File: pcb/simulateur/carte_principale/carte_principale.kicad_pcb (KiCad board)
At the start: 2 copper layers, 54.5 x 50 mm, 25 parts, among them J1 Arduino_UNO_R3, J2 Conn_01x02, J3 Conn_01x02, P1 TE-FFC-10-0.5, P2 TE-FFC-10-0.5, U1 ESP-WROOM-02, U2 LSM6DS3, U3 BMP280, U5 74AHC1G125, U6 74LS166, U7 LIS2MDL

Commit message: carte principale simulateur en cours
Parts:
- removed C10: 220nF, Capacitor_SMD:C_1206_3216Metric
- removed JP1, JP2, JP3: SJ, Jumper:SolderJumper-2_P1.3mm_Open_RoundedPad1.0x1.5mm
- removed P1, P2: TE-FFC-10-0.5, Insa:FFC-10-0.5
- removed R1, R2: 10K, Resistor_SMD:R_1206_3216Metric
- added C8: 100nF, Capacitor_SMD:C_1206_3216Metric_Pad1.42x1.75mm_HandSolder, F.Cu at (126.0, 92.5)
- added C9: 100nF, Capacitor_SMD:C_1206_3216Metric_Pad1.42x1.75mm_HandSolder, F.Cu at (109.0, 79.5)
- added D1: CSA2D-E3/I, Diode_SMD:D_SMA_Handsoldering, F.Cu at (101.0, 100.0)
- added D2: 3.3V, Diode_SMD:D_SMA_Handsoldering, F.Cu at (129.5, 80.0)
- added F1: Littefuse 72R075U, Capacitor_THT:C_Disc_D7.0mm_W2.5mm_P5.00mm, F.Cu at (98.5, 104.0)
- added R10: 1.5K, Resistor_SMD:R_1206_3216Metric_Pad1.42x1.75mm_HandSolder, F.Cu at (132.0, 90.0)
- added R11: 1.5K, Resistor_SMD:R_1206_3216Metric_Pad1.42x1.75mm_HandSolder, F.Cu at (127.5, 83.5)
- added R12: 100, Resistor_SMD:R_1206_3216Metric_Pad1.42x1.75mm_HandSolder, F.Cu at (104.0, 91.0)
- added R13: 100, Resistor_SMD:R_1206_3216Metric_Pad1.42x1.75mm_HandSolder, F.Cu at (110.0, 92.0)
- added R14: 100, Resistor_SMD:R_1206_3216Metric_Pad1.42x1.75mm_HandSolder, F.Cu at (110.0, 85.5)
- added R15: 100, Resistor_SMD:R_1206_3216Metric_Pad1.42x1.75mm_HandSolder, F.Cu at (109.0, 82.0)
- added R16: 100, Resistor_SMD:R_1206_3216Metric_Pad1.42x1.75mm_HandSolder, F.Cu at (134.5, 94.0)
- added R17: 100, Resistor_SMD:R_1206_3216Metric_Pad1.42x1.75mm_HandSolder, F.Cu at (134.5, 96.5)
- added R18: 100, Resistor_SMD:R_1206_3216Metric_Pad1.42x1.75mm_HandSolder, F.Cu at (116.0, 83.0)
- added R19: 100, Resistor_SMD:R_1206_3216Metric_Pad1.42x1.75mm_HandSolder, F.Cu at (122.0, 81.0)
- added R3: 16K, Resistor_SMD:R_1206_3216Metric_Pad1.42x1.75mm_HandSolder, F.Cu at (128.0, 104.0)
- added R4: 330, Resistor_SMD:R_1206_3216Metric_Pad1.42x1.75mm_HandSolder, F.Cu at (118.5, 99.5)
- added R5: 1K, Resistor_SMD:R_1206_3216Metric_Pad1.42x1.75mm_HandSolder, F.Cu at (132.5, 84.0)
- added R6: 1K, Resistor_SMD:R_1206_3216Metric_Pad1.42x1.75mm_HandSolder, F.Cu at (136.5, 78.0)
- added R7: 100, Resistor_SMD:R_1206_3216Metric_Pad1.42x1.75mm_HandSolder, F.Cu at (133.0, 87.0)
- added R8: 1.5K, Resistor_SMD:R_1206_3216Metric_Pad1.42x1.75mm_HandSolder, F.Cu at (127.5, 89.0)
- added R9: 1.5K, Resistor_SMD:R_1206_3216Metric_Pad1.42x1.75mm_HandSolder, F.Cu at (127.0, 85.5)
- added U4: 74LVC2G17, Package_TO_SOT_SMD:SOT-23-6_Handsoldering, F.Cu at (103.5, 87.0)
- C1: value 100nF -> 10µF; footprint Capacitor_SMD:C_1206_3216Metric -> Capacitor_Tantalum_SMD:CP_EIA-3528-21_Kemet-B_Pad1.50x2.35mm_HandSolder
- C2: value 100nF -> 100µF; footprint Capacitor_SMD:C_1206_3216Metric -> Capacitor_Tantalum_SMD:CP_EIA-3528-21_Kemet-B_Pad1.50x2.35mm_HandSolder
- C3: value 100nF -> 10µF; footprint Capacitor_SMD:C_1206_3216Metric -> Capacitor_SMD:C_1206_3216Metric_Pad1.42x1.75mm_HandSolder
- C4, C5, C6, C7: footprint Capacitor_SMD:C_1206_3216Metric -> Capacitor_SMD:C_1206_3216Metric_Pad1.42x1.75mm_HandSolder
- J2: value Conn_01x02 -> Conn_02x08_Odd_Even; footprint Connector_PinHeader_2.54mm:PinHeader_1x02_P2.54mm_Vertical -> Connector_Multicomp:Multicomp_MC9A12-1634_2x08_P2.54mm_Vertical
- J3: footprint Connector_PinHeader_2.54mm:PinHeader_1x02_P2.54mm_Vertical -> TerminalBlock:TerminalBlock_bornier-2_P5.08mm
- U1: value ESP-WROOM-02 -> LM1117MPX-3.3; footprint RF_Module:ESP-WROOM-02 -> Package_TO_SOT_SMD:SOT-223-3_TabPin2
- U2: value LSM6DS3 -> TSV911AILT; footprint Insa:LGA-14_3x2.5mm_P0.5mm_LayoutBorder3x4y-slim -> Package_TO_SOT_SMD:SOT-23-5
- U3: value BMP280 -> ISO1540; footprint Package_LGA:Bosch_LGA-8_2x2.5mm_P0.65mm_ClockwisePinNumbering -> Package_SO:SOIC-8_3.9x4.9mm_P1.27mm
- U5: value 74AHC1G125 -> 74LVC2G17; footprint Package_TO_SOT_SMD:SOT-353_SC-70-5 -> Package_TO_SOT_SMD:SOT-23-6_Handsoldering
- U6: value 74LS166 -> 74LVC2G17; footprint Package_SO:SOIC-16_3.9x9.9mm_P1.27mm -> Package_TO_SOT_SMD:SOT-23-6_Handsoldering
- U7: value LIS2MDL -> 74LVC2G17; footprint Insa:LGA-12_2x2mm_P0.5mm-slim -> Package_TO_SOT_SMD:SOT-23-6_Handsoldering
- moved J3 50.9 mm to (98.5, 110.0)
- moved U1 35.8 mm to (112.0, 105.5)
- moved C7 31.1 mm to (121.5, 77.5), turned to 0 degrees
- moved U7 28.8 mm to (117.0, 80.0)
- moved C3 28.0 mm to (129.5, 100.5)
- moved C5 26.8 mm to (123.0, 105.0)
- moved U3 24.9 mm to (121.0, 86.0), turned to 0 degrees
- moved C2 21.1 mm to (107.5, 96.0), turned to 0 degrees
- moved C1 19.7 mm to (100.5, 95.5), turned to 0 degrees
- moved U6 19.1 mm to (103.5, 80.5), turned to 0 degrees
- moved C4 14.8 mm to (121.5, 90.5), turned to 0 degrees
- moved U5 13.8 mm to (120.5, 94.0), turned to 0 degrees
- moved C6 10.1 mm to (110.0, 87.0)
- moved J2 9.54 mm to (108.0, 71.5)
- moved U2 6.92 mm to (123.5, 100.5), turned to 0 degrees
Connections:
- C1 pad 1: VCC -> +9V
- C2 pad 1: VCC -> +3V3
- C3 pad 1: VCC -> Net-(C3-Pad1)
- C4 pad 1: VCC -> +3V3
- C5 pad 1: VCC -> +3V3
- C6 pad 1: VCC -> +3V3
- C7 pad 1: VCC -> +3V3
- J1 pad 1: Net-(J1-Pad1) -> (no net)
- J1 pad 10: Net-(J1-Pad10) -> /SIM_CARD_DETECT
- J1 pad 11: Net-(J1-Pad11) -> (no net)
- J1 pad 12: Net-(J1-Pad12) -> (no net)
- J1 pad 13: Net-(J1-Pad13) -> (no net)
- J1 pad 14: Net-(J1-Pad14) -> (no net)
- J1 pad 15: /WIFI_TX -> /SIM_UART_TX
- J1 pad 16: /WIFI_RX -> /SIM_UART_RX
- J1 pad 17: /WIFI_EN -> /SIM_GYRO_IDX
- J1 pad 18: /WIFI_RST -> /SIM_MOT_PWM
- J1 pad 19: /KEYS_EN -> /SIM_GYRO_PHB
- J1 pad 2: Net-(J1-Pad2) -> (no net)
- J1 pad 20: /LSM6DS3_IT -> /SIM_VBAT
- J1 pad 21: /LIS2MDL_IT -> /SIM_SERVO_PWM
- J1 pad 22: Net-(J1-Pad22) -> /SIM_GYRO_PHA
- J1 pad 23: Net-(J1-Pad23) -> /SIM_MOT_DIR
- J1 pad 24: /KEYS_LOAD -> (no net)
- J1 pad 25: /BMP280_EN -> (no net)
- J1 pad 26: /SPI_MOSI -> (no net)
- J1 pad 27: /SPI_MISO -> (no net)
- J1 pad 28: /SPI_SCK -> (no net)
- J1 pad 3: /KEY_RST -> (no net)
- J1 pad 30: Net-(J1-Pad30) -> (no net)
- J1 pad 31: /I2C_SDA -> /SIM_CAPTEURS_SDA
- J1 pad 32: /I2C_SCL -> /SIM_CAPTEURS_SCL
- J1 pad 4: VCC -> (no net)
- J1 pad 5: Net-(J1-Pad5) -> (no net)
- J1 pad 8: Net-(J1-Pad8) -> +9V
- J1 pad 9: Net-(J1-Pad9) -> (no net)
- J2 pad 1: /Audio_Left_2 -> GND
- J2 pad 2: /Audio_Left_1 -> +3V3
- J3 pad 1: /Audio_Right_2 -> GND
- J3 pad 2: /Audio_Right_1 -> Net-(F1-Pad2)
- U1 pad 1: VCC -> GND
- U1 pad 2: /WIFI_EN -> +3V3
- U1 pad 3: Net-(U1-Pad3) -> +9V
- U2 pad 1: VCC -> Net-(R4-Pad2)
- U2 pad 2: Net-(U2-Pad2) -> GND
- U2 pad 3: Net-(U2-Pad3) -> Net-(C3-Pad1)
- U2 pad 4: Net-(JP1-Pad1) -> Net-(R4-Pad2)
- U2 pad 5: VCC -> +3V3
- U3 pad 1: GND -> +3V3
- U3 pad 2: /BMP280_EN -> /CAPTEURS_SDA
- U3 pad 3: /SPI_MOSI -> /CAPTEURS_SCL
- U3 pad 4: /SPI_SCK -> GND
- U3 pad 5: /SPI_MISO -> GND
- U3 pad 6: VCC -> /SIM_CAPTEURS_SCL
- U3 pad 7: GND -> /SIM_CAPTEURS_SDA
- U3 pad 8: VCC -> +3V3
- U5 pad 1: /KEYS_EN -> Net-(R14-Pad2)
- U5 pad 2: Net-(U5-Pad2) -> GND
- U5 pad 3: GND -> Net-(R15-Pad2)
- U5 pad 4: /SPI_MISO -> /SIM_UART_TX
- U5 pad 5: VCC -> +3V3
- U6 pad 1: VCC -> /SIM_GYRO_PHA
- U6 pad 2: /Key_B -> GND
- U6 pad 3: /Key_A -> /SIM_GYRO_PHB
- U6 pad 4: /Key_Y -> Net-(R17-Pad1)
- U6 pad 5: /Key_X -> +3V3
- U6 pad 6: /KEYS_EN -> Net-(R16-Pad1)
- U7 pad 1: /I2C_SCL -> /SIM_GYRO_IDX
- U7 pad 2: Net-(U7-Pad2) -> GND
- U7 pad 3: VCC -> /SIM_UART_RX
- U7 pad 4: /I2C_SDA -> Net-(R19-Pad1)
- U7 pad 5: Net-(C10-Pad1) -> +3V3
- U7 pad 6: GND -> Net-(R18-Pad1)
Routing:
- net GND: track 254.0 -> 0.00 mm, vias 8 -> 0
- net VCC: track 248.9 -> 0.00 mm, vias 11 -> 0
- net /LSM6DS3_IT: track 138.6 -> 0.00 mm, vias 2 -> 0
- net /KEYS_EN: track 74.0 -> 0.00 mm, vias 3 -> 0
- net /SPI_SCK: track 70.3 -> 0.00 mm, vias 1 -> 0
- net /LIS2MDL_IT: track 54.9 -> 0.00 mm
- net /WIFI_RST: track 51.0 -> 0.00 mm, vias 2 -> 0
- net /WIFI_TX: track 50.4 -> 0.00 mm, vias 1 -> 0
- net /I2C_SDA: track 45.5 -> 0.00 mm, vias 3 -> 0
- net /SPI_MISO: track 44.9 -> 0.00 mm, vias 2 -> 0
- net /I2C_SCL: track 40.4 -> 0.00 mm
- net /WIFI_RX: track 40.4 -> 0.00 mm, vias 1 -> 0
- net /KEYS_LOAD: track 32.5 -> 0.00 mm, vias 1 -> 0
- net /Audio_Right_2: track 28.6 -> 0.00 mm, vias 1 -> 0
- net /Audio_Right_1: track 25.1 -> 0.00 mm, vias 1 -> 0
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- removed copper zone on B.Cu, net GND
- removed copper zone on F.Cu, net GND
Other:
- board text added: "GEI"
- board text added: "V 1.0"
- board text removed: "STPI"
- board text removed: "V 02C"

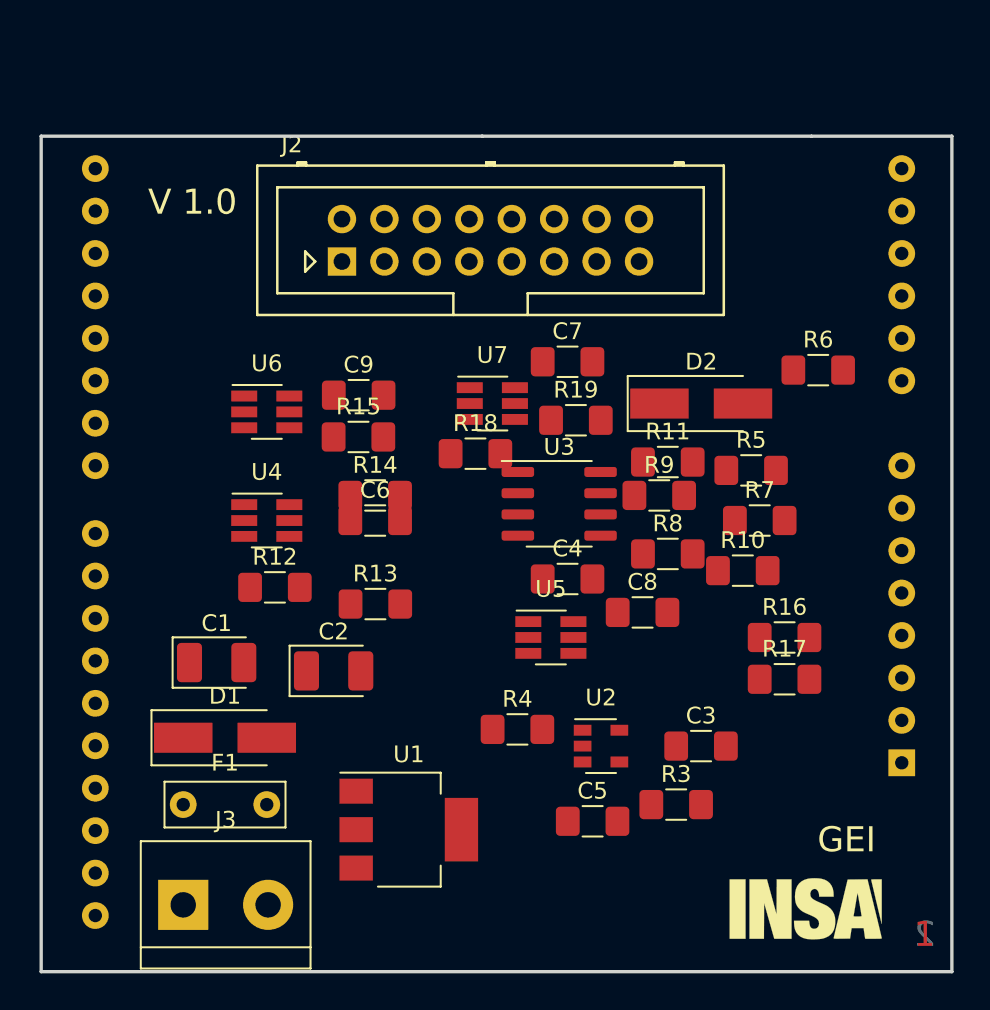
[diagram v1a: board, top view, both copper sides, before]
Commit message: modification sur la carte principale du simulateur + redaction des lignes I/O utilisées entre la carte etudiant et le bateau
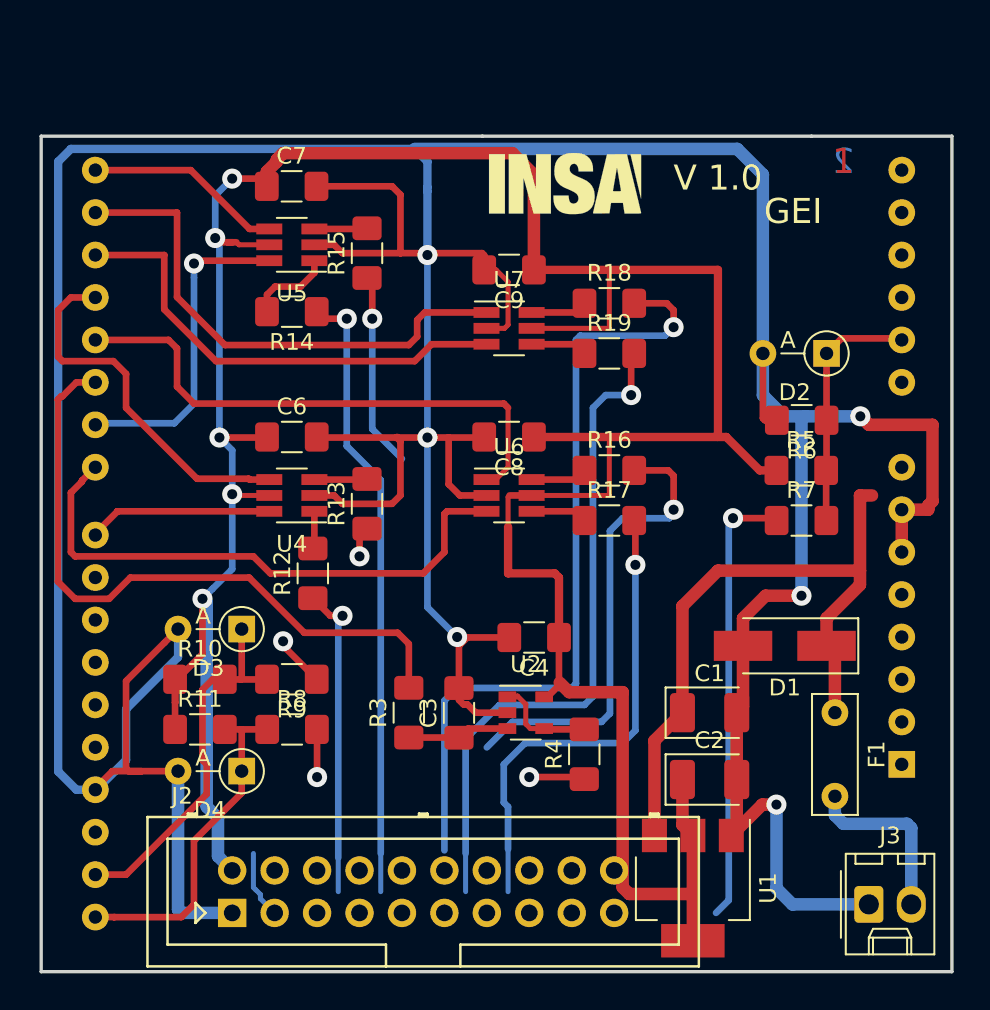
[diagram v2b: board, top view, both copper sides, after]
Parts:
- removed C5: 100nF, Capacitor_SMD:C_1206_3216Metric_Pad1.42x1.75mm_HandSolder
- removed U3: ISO1540, Package_SO:SOIC-8_3.9x4.9mm_P1.27mm
- added D3: 3.6V, Diode_THT:D_DO-35_SOD27_P3.81mm_Vertical_AnodeUp, F.Cu at (102.0, 93.5)
- added D4: 3.6V, Diode_THT:D_DO-35_SOD27_P3.81mm_Vertical_AnodeUp, F.Cu at (102.0, 102.0)
- D2: value 3.3V -> 3.6V; footprint Diode_SMD:D_SMA_Handsoldering -> Diode_THT:D_DO-35_SOD27_P3.81mm_Vertical_AnodeUp
- J2: value Conn_02x08_Odd_Even -> Conn_02x10_Odd_Even; footprint Connector_Multicomp:Multicomp_MC9A12-1634_2x08_P2.54mm_Vertical -> Connector_Multicomp:Multicomp_MC9A12-2034_2x10_P2.54mm_Vertical
- J3: footprint TerminalBlock:TerminalBlock_bornier-2_P5.08mm -> Connector_Molex:Molex_KK-254_AE-6410-02A_1x02_P2.54mm_Vertical
- R10, R11: value 1.5K -> 3.3K
- R12, R13, R14, R15, R16, R17, R18, R19, R7: value 100 -> 330
- R8, R9: value 1.5K -> 330
- U1: value LM1117MPX-3.3 -> AMS1117-3.3
- moved Logo1 45.7 mm to (121.5, 67.0)
- moved J3 41.0 mm to (139.5, 110.0)
- moved J2 39.5 mm to (101.4, 110.5)
- moved F1 39.4 mm to (137.5, 98.5), turned to 270 degrees
- moved D1 33.9 mm to (134.5, 94.5), turned to 180 degrees
- moved R10 33.1 mm to (99.5, 96.5)
- moved R11 32.2 mm to (99.5, 99.5)
- moved C1 29.7 mm to (130.0, 98.5)
- moved U5 28.2 mm to (105.0, 70.5), turned to 180 degrees
- moved R8 24.8 mm to (105.0, 99.5)
- moved R9 24.6 mm to (105.0, 96.5), turned to 180 degrees
- moved C2 23.4 mm to (130.0, 102.5)
- moved C7 19.6 mm to (105.0, 67.0)
- moved U1 17.4 mm to (129.0, 109.0), turned to 270 degrees
- moved R3 16.9 mm to (112.0, 98.5), turned to 90 degrees
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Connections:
- net /GYRO_INDEX renamed /XBEE_UART_RX
- net /SIM_VBAT renamed /SIM_V_BATTERIE
- C1 pad 1: +9V -> +5V
- D1 pad 1: +9V -> +5V
- F1 pad 1: +9V -> +5V
- J1 pad 17: /SIM_GYRO_IDX -> /SIM_GIRO_IDX
- J1 pad 19: /SIM_GYRO_PHB -> /SIM_GIRO_PHB
- J1 pad 22: /SIM_GYRO_PHA -> /SIM_GIRO_PHA
- J1 pad 5: (no net) -> +5V
- J1 pad 8: +9V -> (no net)
- J2 pad 11: /CAPTEURS_SDA -> /GIRO_PHA
- J2 pad 12: /CAPTEURS_SCL -> /GIRO_PHB
- J2 pad 13: /UART_TX -> /CARD_DETECT
- J2 pad 14: /UART_RX -> /TENSION_BATTERIE
- J2 pad 15: /VBAT -> (no net)
- J2 pad 16: /CARD_DETECT -> (no net)
- J2 pad 3: GND -> /CAPTEURS_SDA
- J2 pad 4: +3V3 -> /CAPTEURS_SCL
- J2 pad 5: /MOT_PWM -> /MOT_DIR
- J2 pad 6: /MOT_DIR -> /MOT_PWM
- J2 pad 8: /GYRO_PHA -> /XBEE_UART_TX
- J2 pad 9: /GYRO_PHB -> /GIRO_INDEX
- R12 pad 1: /MOT_PWM -> /MOT_DIR
- R13 pad 1: /MOT_DIR -> /MOT_PWM
- R15 pad 1: /UART_TX -> /XBEE_UART_TX
- R16 pad 2: /GYRO_PHA -> /GIRO_PHB
- R17 pad 2: /GYRO_PHB -> /GIRO_PHA
- R19 pad 2: /UART_RX -> /GIRO_INDEX
- R4 pad 1: /VBAT -> /TENSION_BATTERIE
- R8 pad 1: +3V3 -> /SIM_CAPTEURS_SCL
- R8 pad 2: /CAPTEURS_SDA -> /CAPTEURS_SCL
- R9 pad 1: +3V3 -> /CAPTEURS_SDA
- R9 pad 2: /CAPTEURS_SCL -> /SIM_CAPTEURS_SDA
- U1 pad 3: +9V -> +5V
- U4 pad 4: /SIM_MOT_DIR -> /SIM_MOT_PWM
- U4 pad 6: /SIM_MOT_PWM -> /SIM_MOT_DIR
- U6 pad 1: /SIM_GYRO_PHA -> /SIM_GIRO_PHB
- U6 pad 3: /SIM_GYRO_PHB -> /SIM_GIRO_PHA
- U7 pad 1: /SIM_GYRO_IDX -> /SIM_UART_RX
- U7 pad 3: /SIM_UART_RX -> /SIM_GIRO_IDX
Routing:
- net GND: track 0.00 -> 293.2 mm, vias 0 -> 6
- net +3V3: track 0.00 -> 188.2 mm, vias 0 -> 5
- net /XBEE_UART_RX: track 0.00 -> 47.5 mm, vias 0 -> 1
- net +5V: track 0.00 -> 40.7 mm
- net /GIRO_INDEX: track 0.00 -> 40.3 mm, vias 0 -> 1
- net /SIM_V_BATTERIE: track 0.00 -> 39.8 mm
- net /SERVO_PWM: track 0.00 -> 37.1 mm, vias 0 -> 1
- net /SIM_GIRO_PHA: track 0.00 -> 34.0 mm
- net /SIM_GIRO_PHB: track 0.00 -> 32.9 mm
- net /SIM_UART_RX: track 0.00 -> 31.1 mm
- net /GIRO_PHA: track 0.00 -> 29.0 mm, vias 0 -> 1
- net /SIM_GIRO_IDX: track 0.00 -> 28.4 mm
- net /GIRO_PHB: track 0.00 -> 28.1 mm, vias 0 -> 1
- net /CARD_DETECT: track 0.00 -> 26.7 mm, vias 0 -> 1
- net /SIM_MOT_PWM: track 0.00 -> 22.3 mm
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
